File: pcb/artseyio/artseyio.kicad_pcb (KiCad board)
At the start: 2 copper layers, 76.2 x 73.7 mm, 21 parts, among them J1 USB_C16PIN, J2 BOOT, SW1 SW_MEC_5G, SW2 SW_MEC_5G, SW3 SW_MEC_5G, SW4 SW_MEC_5G, SW5 SW_MEC_5G, SW6 SW_MEC_5G, SW7 SW_MEC_5G, SW8 SW_MEC_5G, U3 CH552G

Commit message: Reverted PCB also.
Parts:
- removed R1, R2, R3, R4: 5.1k, Resistor_SMD:R_0805_2012Metric
- J2: value BOOT -> RST
- moved H1 1.27 mm to (123.2, 59.7)
- moved H2 1.27 mm to (123.2, 120.7)
- moved H3 1.27 mm to (184.2, 59.7)
- moved H4 1.27 mm to (184.2, 120.7)
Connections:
- net /D+ renamed Net-(J1-PadA6)
- C2 pad 2: /3.3v -> Net-(U3-Pad16)
- J2 pad 2: /3.3v -> Earth
- U3 pad 16: /3.3v -> Net-(U3-Pad16)
- U3 pad 2: unconnected-(U3-Pad2) -> /CC1
- U3 pad 3: unconnected-(U3-Pad3) -> /CC2
- U3 pad 6: unconnected-(U3-Pad6) -> Net-(J2-Pad1)
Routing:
- net /3.3v: track 24.9 -> 0.00 mm, vias 1 -> 0
- net /CC2: track 3.31 -> 22.1 mm, vias 0 -> 2
- net /CC1: track 6.39 -> 18.4 mm
- net Net-(J1-PadA6): track 35.4 -> 25.6 mm
- net /R: track 50.0 -> 55.6 mm
- net Net-(J2-Pad1): track 3.85 -> 8.81 mm
- net Earth: track 36.3 -> 32.0 mm, vias 2 -> 1
- net Net-(U3-Pad16): track 0.00 -> 4.03 mm
- net Net-(R3-Pad1): track 3.04 -> 0.00 mm
- net unconnected-(U3-Pad2): track 1.38 -> 0.00 mm
- net unconnected-(U3-Pad6): track 0.76 -> 0.00 mm
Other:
- board size 76.2 x 73.7 mm -> 76.2 x 76.2 mm
- board text added: "RST"
- board text removed: "BOOT"

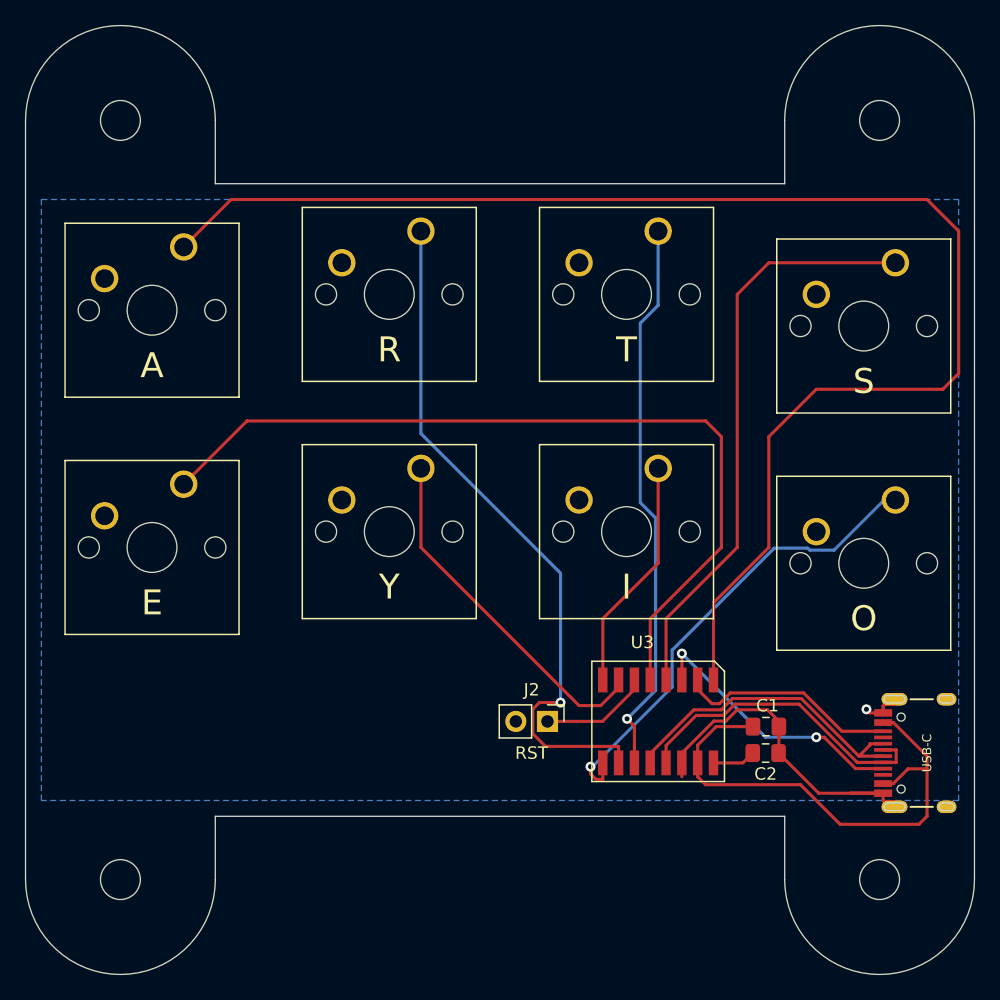
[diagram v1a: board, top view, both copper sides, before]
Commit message: Filled out v1.1 design with boot jumper and correct cc line pulldowns.
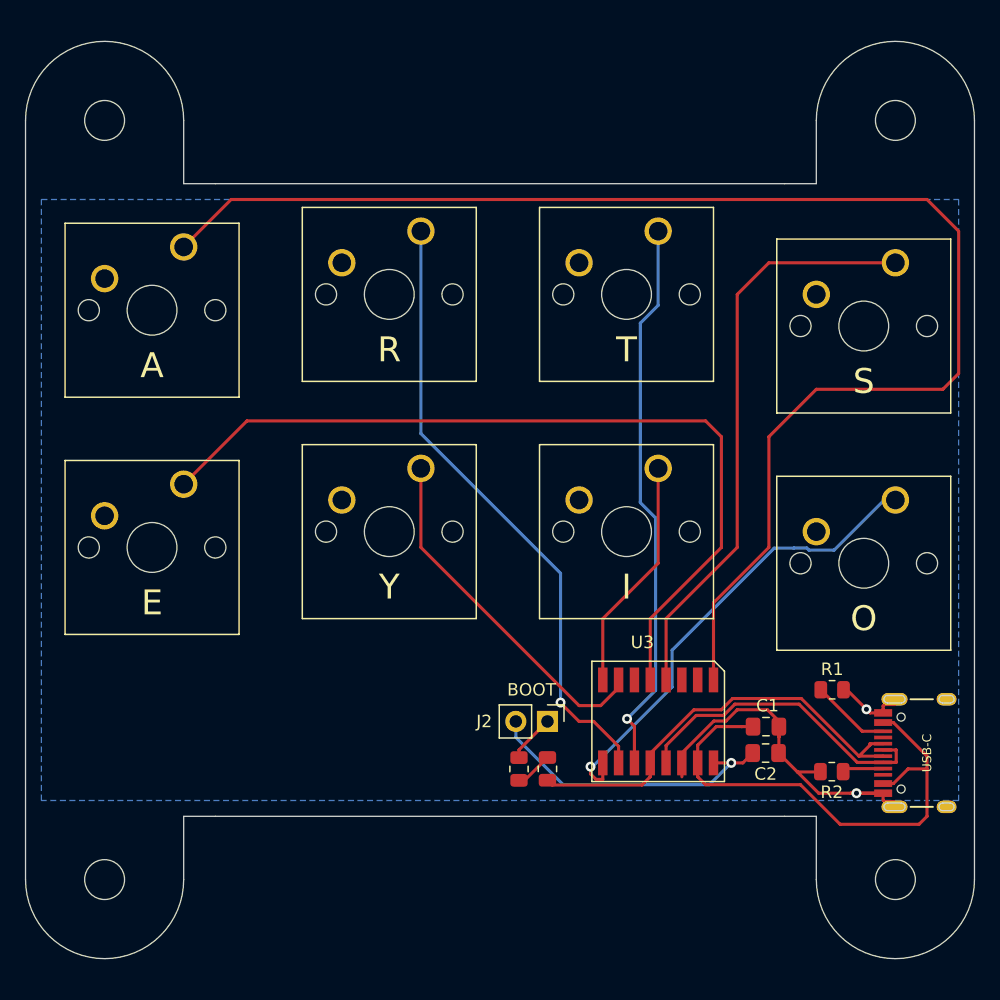
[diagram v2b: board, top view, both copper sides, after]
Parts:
- added R1: 5.1k, Resistor_SMD:R_0805_2012Metric, F.Cu at (180.3, 105.4)
- added R2: 5.1k, Resistor_SMD:R_0805_2012Metric, F.Cu at (180.3, 112.0)
- added R3: 5.1k, Resistor_SMD:R_0805_2012Metric, F.Cu at (157.5, 111.8)
- added R4: 5.1k, Resistor_SMD:R_0805_2012Metric, F.Cu at (155.2, 111.8)
- J2: value RST -> BOOT
- moved H1 1.27 mm to (121.9, 59.7)
- moved H2 1.27 mm to (121.9, 120.7)
- moved H3 1.27 mm to (185.4, 59.7)
- moved H4 1.27 mm to (185.4, 120.7)
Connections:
- net Net-(J1-PadA6) renamed /D+
- C2 pad 2: Net-(U3-Pad16) -> /3.3v
- J2 pad 2: Earth -> /3.3v
- U3 pad 16: Net-(U3-Pad16) -> /3.3v
- U3 pad 2: /CC1 -> unconnected-(U3-Pad2)
- U3 pad 3: /CC2 -> unconnected-(U3-Pad3)
- U3 pad 6: Net-(J2-Pad1) -> unconnected-(U3-Pad6)
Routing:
- net /3.3v: track 0.00 -> 24.9 mm, vias 0 -> 1
- net /CC2: track 22.1 -> 3.31 mm, vias 2 -> 0
- net /CC1: track 18.4 -> 6.39 mm
- net /D+: track 25.6 -> 35.4 mm
- net /R: track 55.6 -> 50.0 mm
- net Net-(J2-Pad1): track 8.81 -> 3.85 mm
- net Earth: track 32.0 -> 36.3 mm, vias 1 -> 2
- net Net-(U3-Pad16): track 4.03 -> 0.00 mm
- net Net-(R3-Pad1): track 0.00 -> 3.04 mm
- net unconnected-(U3-Pad2): track 0.00 -> 1.38 mm
- net unconnected-(U3-Pad6): track 0.00 -> 0.76 mm
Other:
- board size 76.2 x 76.2 mm -> 76.2 x 73.7 mm
- board text added: "BOOT"
- board text removed: "RST"
